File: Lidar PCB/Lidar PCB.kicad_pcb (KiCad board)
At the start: 2 copper layers, 58 x 69 mm, 48 parts, among them J1 Barrel_Jack, J2 USB_C_Receptacle_USB2.0, J3 Conn_01x02_Socket, J4 Conn_01x06_Pin, J5 Conn_01x06_Socket, Q1 IRF740, SW1 SW_Push, U1 AMS1117-5.0, U2 ATmega328P-A, U3 FT232RL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

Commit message: Included information silkscreen on PCB
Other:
- board text added: "Designed by Alan Carvalho"
- board text added: "Photon Lidar V1.0"
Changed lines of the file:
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@@
   (gr_line (start 175.999999 126.999999) (end 176 90)
     (stroke (width 0.5) (type default)) (layer "Edge.Cuts"))
+  (gr_text "Photon Lidar V1.0" (at 147 110.998) (layer "B.SilkS")
+    (effects (font (size 3 3) (thickness 0.6) bold) (justify mirror))
+  )
+  (gr_text "Designed by Alan Carvalho" (at 167.386 115.824) (layer "B.SilkS")
+    (effects (font (size 1.5 1.5) (thickness 0.3) bold) (justify left bottom mirror))
+  )
   (segment (start 132.334 83.82) (end 132.334 86.36) (width 0.5) (layer "F.Cu") (net 1))
   (segment (start 140.208 75.946) (end 132.334 83.82) (width 0.5) (layer "F.Cu") (net 1))
@@
     )
   )
+  (group "" (id 0fe48891-2964-40a7-9697-8cc4fb09625b)
+    (members
+      2588c8c5-c89d-490c-bc6c-ec4b66aa7327
+      cb42e18d-1722-4f0a-8f05-51cfe430b837
+    )
+  )

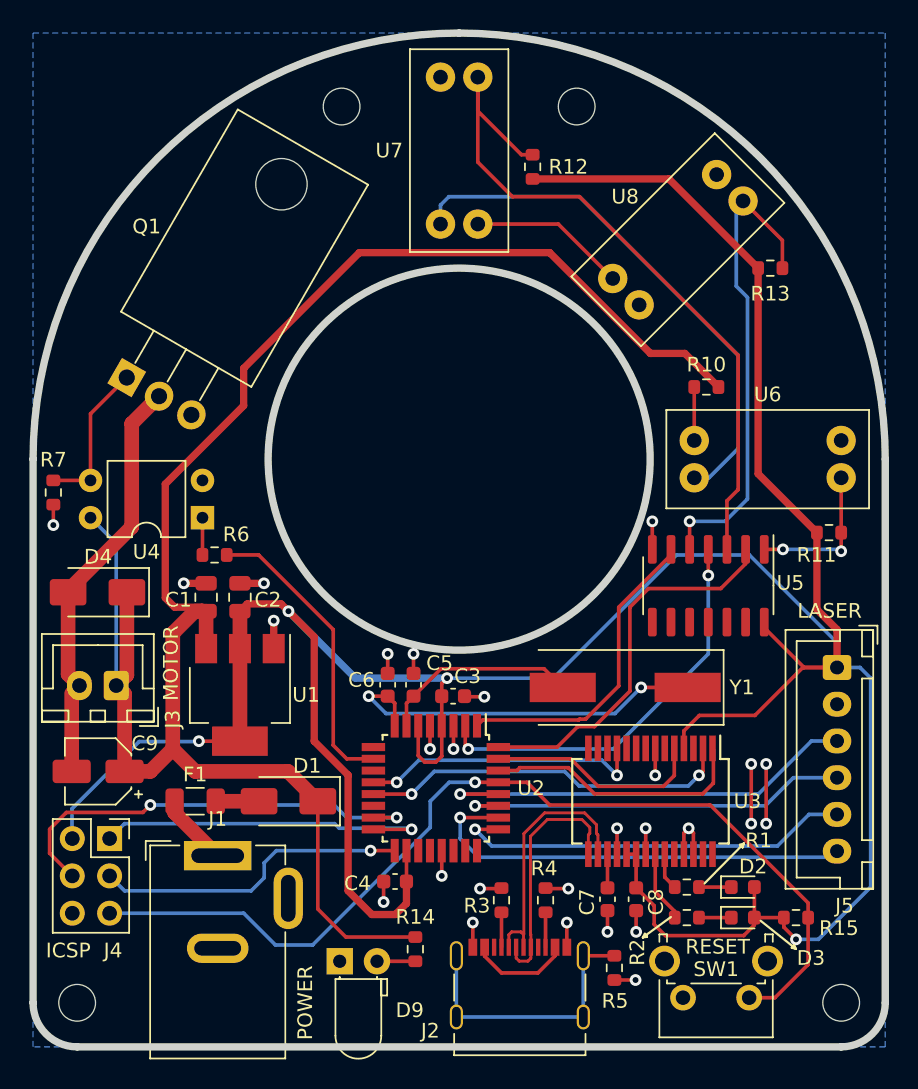
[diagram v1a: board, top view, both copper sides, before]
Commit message: PCB input diode removed
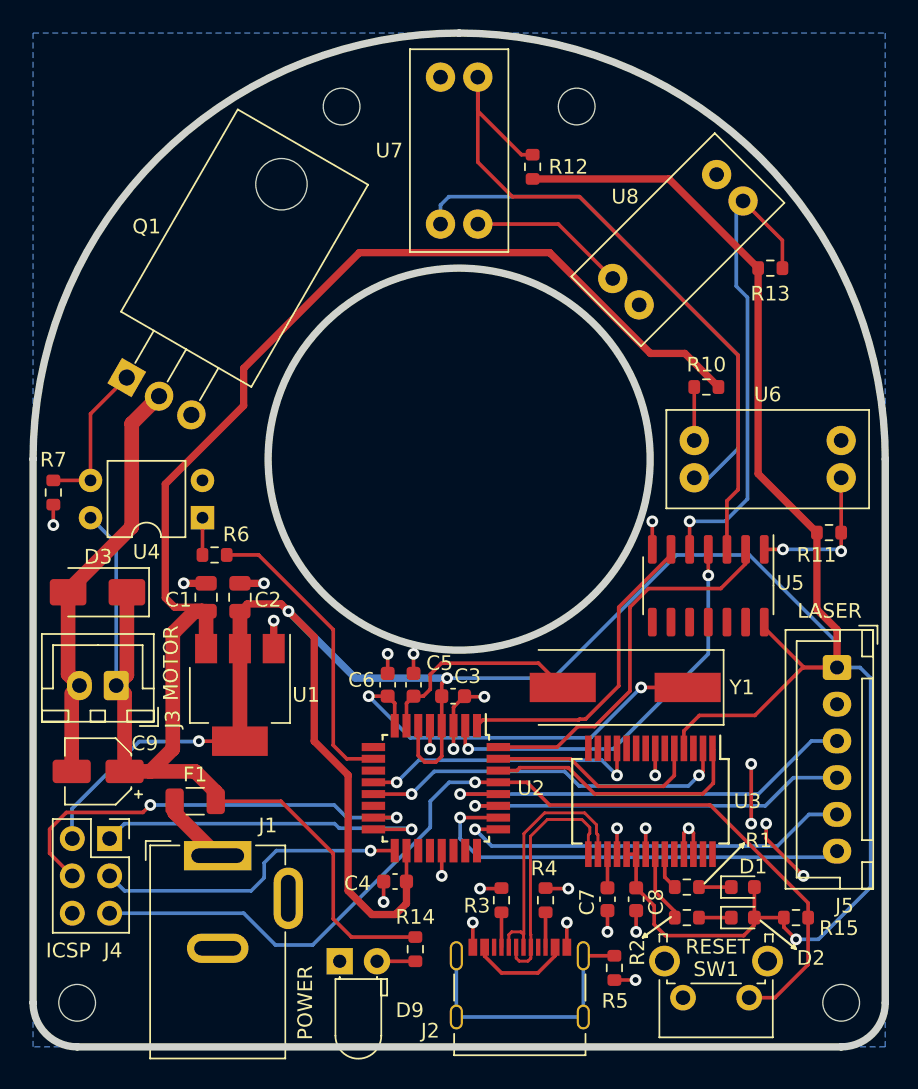
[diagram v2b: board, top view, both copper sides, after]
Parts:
- removed the D1 at (135.4, 113.3)
- renumbered D2 to D1, D3 to D2, D4 to D3
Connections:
- F1 pad 2: Net-(D1-A) -> +12V
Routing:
- net Net-(D1-A): track 2.95 -> 0.00 mm
- net GND: track 46.4 -> 49.3 mm
- net Net-(U2-XTAL2/PB7): track 26.4 -> 27.8 mm
- net Net-(U2-XTAL1/PB6): track 13.7 -> 14.6 mm
